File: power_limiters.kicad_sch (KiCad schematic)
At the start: 31 parts, among them U10 MAX4995AAUT+T, U11 MAX4995AAUT+T, U26 SN74AHC1G08QDCKRQ1, U35 MAX4995AAUT+T, U8 MPQ5072GG-AEC1-Z, U9 MAX4995AAUT+T

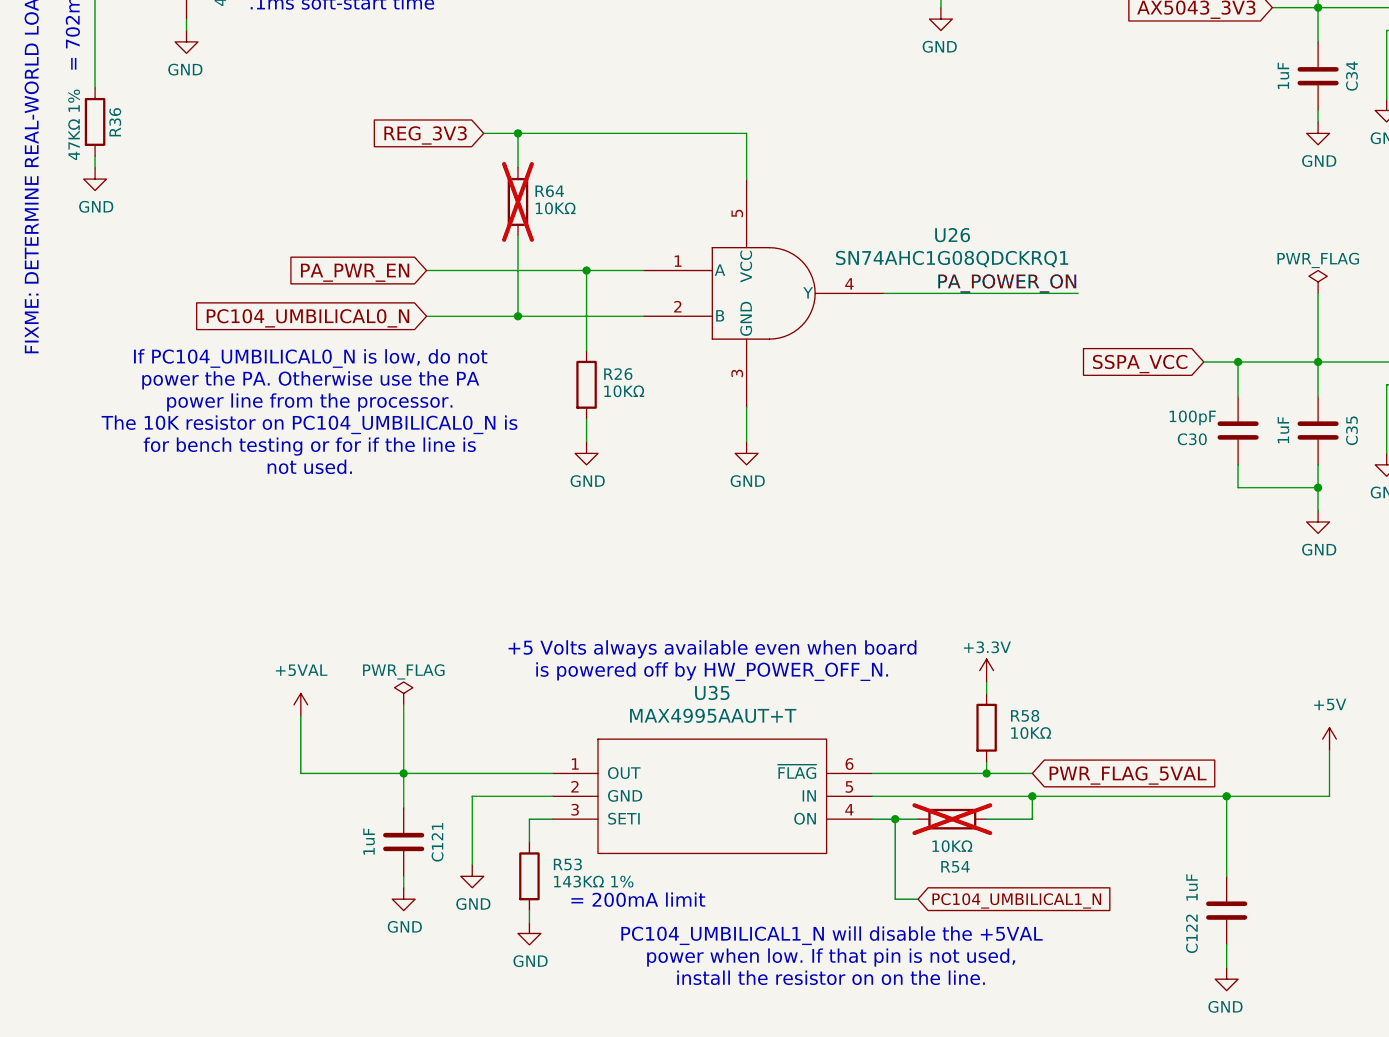
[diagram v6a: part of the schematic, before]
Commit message: Rework the ABF/Umbilical lines
It turns out these do not work as I thought.

Move the inhibits to separate pins and rework it a bit.  It now has two
inhibits, plus the HW_POWER_EN one for a third.

The ABF line is now run to a GPIO.

Signed-off-by: Corey Minyard <corey@minyard.net>
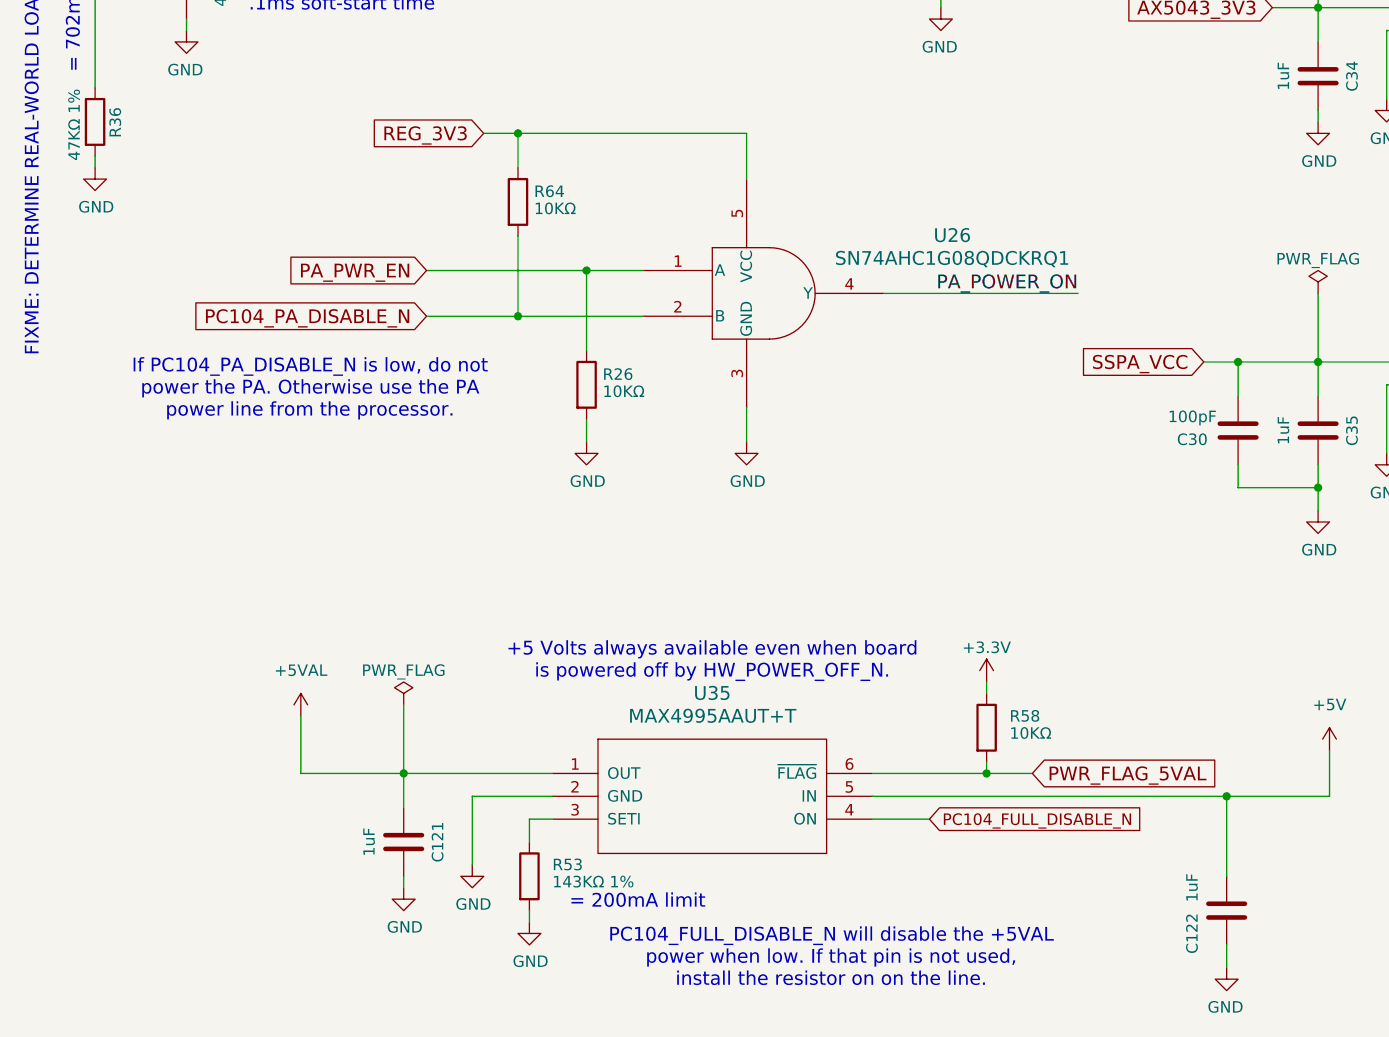
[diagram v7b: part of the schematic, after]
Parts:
- removed R54: 10KΩ, Resistor_SMD:R_0402_1005Metric_Pad0.72x0.64mm_HandSolder, symbol Device:R
- R64: now fitted; now in the parts list
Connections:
- net PC104_UMBILICAL0_N renamed PC104_PA_DISABLE_N
- net PC104_UMBILICAL1_N renamed PC104_FULL_DISABLE_N
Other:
- note added: "If PC104_PA_DISABLE_N is low, do not power the PA. Otherwise use the PA power line from the processor."
- note added: "PC104_FULL_DISABLE_N will disable the +5VAL power when low. If that pin is not used, install the resistor on on the line."
- note removed: "If PC104_UMBILICAL0_N is low, do not power the PA. Otherwise use the PA power line from the processor. The 10K resistor on PC104_UMBILICAL0_N is for bench testing or for if the line is not used."
- note removed: "PC104_UMBILICAL1_N will disable the +5VAL power when low. If that pin is not used, install the resistor on on the line."
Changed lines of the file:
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@@
 		)
 	)
-	(text "If PC104_UMBILICAL0_N is low, do not\npower the PA. Otherwise use the PA\npower line from the processor.\nThe 10K resistor on PC104_UMBILICAL0_N is\nfor bench testing or for if the line is\nnot used."
+	(text "If PC104_PA_DISABLE_N is low, do not\npower the PA. Otherwise use the PA\npower line from the processor."
 		(exclude_from_sim no)
-		(at 50.546 122.682 0)
+		(at 50.546 119.888 0)
 		(effects
 			(font
@@
 		)
 	)
-	(text "PC104_UMBILICAL1_N will disable the +5VAL\npower when low. If that pin is not used,\ninstall the resistor on on the line."
+	(text "PC104_FULL_DISABLE_N will disable the +5VAL\npower when low. If that pin is not used,\ninstall the resistor on on the line."
 		(exclude_from_sim no)
 		(at 108.458 183.134 0)
@@
 	)
 	(junction
-		(at 130.81 165.1)
-		(diameter 0)
-		(color 0 0 0 0)
-	)
-	(junction
 		(at 257.81 67.31)
 		(diameter 0)
@@
 	)
 	(junction
-		(at 115.57 167.64)
-		(diameter 0)
-		(color 0 0 0 0)
-	)
-	(junction
 		(at 99.06 64.77)
 		(diameter 0)
@@
 	(wire
 		(pts
-			(xy 113.03 165.1) (xy 130.81 165.1)
+			(xy 113.03 165.1) (xy 152.4 165.1)
 		)
 		(stroke
@@
 	(wire
 		(pts
-			(xy 115.57 176.53) (xy 115.57 167.64)
-		)
-		(stroke
-			(width 0)
-			(type default)
-		)
-	)
-	(wire
-		(pts
 			(xy 162.56 41.91) (xy 162.56 38.1)
 		)
@@
 	(wire
 		(pts
-			(xy 115.57 167.64) (xy 118.11 167.64)
-		)
-		(stroke
-			(width 0)
-			(type default)
-		)
-	)
-	(wire
-		(pts
 			(xy 167.64 38.1) (xy 179.07 38.1)
 		)
@@
 	(wire
 		(pts
-			(xy 113.03 167.64) (xy 115.57 167.64)
+			(xy 113.03 167.64) (xy 119.38 167.64)
 		)
 		(stroke
@@
 	(wire
 		(pts
-			(xy 130.81 165.1) (xy 152.4 165.1)
-		)
-		(stroke
-			(width 0)
-			(type default)
-		)
-	)
-	(wire
-		(pts
 			(xy 153.67 130.81) (xy 162.56 130.81)
 		)
@@
 	(wire
 		(pts
-			(xy 118.11 176.53) (xy 115.57 176.53)
-		)
-		(stroke
-			(width 0)
-			(type default)
-		)
-	)
-	(wire
-		(pts
 			(xy 63.5 106.68) (xy 81.28 106.68)
 		)
@@
 	(wire
 		(pts
-			(xy 125.73 167.64) (xy 130.81 167.64)
-		)
-		(stroke
-			(width 0)
-			(type default)
-		)
-	)
-	(wire
-		(pts
 			(xy 81.28 106.68) (xy 87.63 106.68)
 		)
@@
 	(wire
 		(pts
-			(xy 130.81 167.64) (xy 130.81 165.1)
-		)
-		(stroke
-			(width 0)
-			(type default)
-		)
-	)
-	(wire
-		(pts
 			(xy 215.9 73.66) (xy 215.9 77.47)
 		)
@@
 		)
 	)
-	(global_label "PC104_UMBILICAL0_N"
+	(global_label "PC104_PA_DISABLE_N"
 		(shape input)
 		(at 63.5 111.76 180)
@@
 		)
 		(property "Intersheetrefs" "${INTERSHEET_REFS}"
-			(at 36.3194 111.76 0)
+			(at 36.2468 111.76 0)
 			(effects
 				(font
@@
 		)
 	)
-	(global_label "PC104_UMBILICAL1_N"
+	(global_label "PC104_FULL_DISABLE_N"
 		(shape input)
-		(at 118.11 176.53 0)
+		(at 119.38 167.64 0)
 		(fields_autoplaced yes)
 		(effects
@@
 		)
 		(property "Intersheetrefs" "${INTERSHEET_REFS}"
-			(at 140.761 176.53 0)
+			(at 144.2081 167.64 0)
 			(effects
 				(font
@@
 	(symbol
 		(lib_id "Device:R")
-		(at 121.92 167.64 90)
-		(unit 1)
-		(exclude_from_sim no)
-		(in_bom no)
-		(on_board yes)
-		(dnp yes)
-		(property "Reference" "R54"
-			(at 123.952 172.974 90)
-			(effects
-				(font
-					(size 1.27 1.27)
-				)
-				(justify left)
-			)
-		)
-		(property "Value" "10KΩ"
-			(at 124.206 170.688 90)
-			(effects
-				(font
-					(size 1.27 1.27)
-				)
-				(justify left)
-			)
-		)
-		(property "Footprint" "Resistor_SMD:R_0402_1005Metric_Pad0.72x0.64mm_HandSolder"
-			(at 121.92 169.418 90)
-			(effects
-				(font
-					(size 1.27 1.27)
-				)
-				(hide yes)
-			)
-		)
-		(property "Datasheet" "~"
-			(at 122.174 167.64 0)
-			(effects
-				(font
-					(size 1.27 1.27)
-				)
-			)
-		)
-		(property "Description" ""
-			(at 121.92 167.64 0)
-			(effects
-				(font
-					(size 1.27 1.27)
-				)
-			)
-		)
-		(pin "1"
-		)
-		(pin "2"
-		)
-		(instances
-			(project "PacSat_AFSK"
-				(path "/cc9f42d2-6985-41ac-acab-5ab7b01c5b38/00000000-0000-0000-0000-00005a0ea76a/c3879c9c-e3de-4d40-a3e3-f7fd281b7d00"
-					(reference "R54")
-					(unit 1)
-				)
-			)
-		)
-	)
-	(symbol
-		(lib_id "Device:R")
 		(at 215.9 69.85 0)
 		(unit 1)
@@
 		(unit 1)
 		(exclude_from_sim no)
-		(in_bom no)
+		(in_bom yes)
 		(on_board yes)
-		(dnp yes)
+		(dnp no)
 		(property "Reference" "R64"
 			(at 75.438 97.917 0)
